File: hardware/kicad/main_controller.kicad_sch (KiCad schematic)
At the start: 40 parts, among them Q4 DMG1012UW, SW2 B3U-3000P, U1 ESP32-C6FH4, Y1 CM315D32768DZFT, Y2 R940000171

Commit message: hardware/kicad/battery.kicad_sch
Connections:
- net ANT_FEED: now reaches AE1.1 (FEED), C24.2, L4.1
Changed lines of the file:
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@@
 (kicad_sch (version 20230121) (generator eeschema)
   (paper "A4")
+  (title_block
+    (date "2023-10-16")
+    (rev "2")
+  )
   (junction (at 19.05 76.2) (diameter 0) (color 0 0 0 0)
   )
@@
     (effects (font (size 1.27 1.27)) (justify right bottom))
   )
+  (label "ANT_FEED" (at 254.635 27.305 0) (fields_autoplaced)
+    (effects (font (size 1.27 1.27)) (justify left bottom))
+  )
   (label "DL_RXD0" (at 149.86 56.515 180) (fields_autoplaced)

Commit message: wip: removing powergate
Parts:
- removed D2 (x2): RB161QS-40T18R, plantpal:D_0402_1005Metric, symbol Diode:MBR0540
- removed R16: 1M, Resistor_SMD:R_0402_1005Metric, symbol Device:R_Small
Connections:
- net RESET_BTN is gone; now on net CHIP_EN: SW2.1, TP3.1
- net DONE: no longer names the net of U1.11 (MTDI/GPIO5/FSPIWP/ADC1_CH5)
- net M_DRVOUT: no longer names the net of U1.10 (MTMS/GPIO4/FSPIHD/ADC1_CH4)
- no-connect marks 0 -> 2
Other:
- note removed: "Protect from other M_DRV source"

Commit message: wip: revision 2
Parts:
- added Q4: DMG1012UW, Package_TO_SOT_SMD:SOT-323_SC-70, symbol Device:Q_NMOS_GSD
- added R13: 10K, Resistor_SMD:R_0402_1005Metric, symbol Device:R_Small
- added R16: 1M, Resistor_SMD:R_0402_1005Metric, symbol Device:R_Small
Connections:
- net +3V3: now also R13.1
- net GND: now also Q4.2 (S), R16.2
- net MPP_STS_READ: now reaches U1.11 (MTDI/GPIO5/FSPIWP/ADC1_CH5)
- net MPP_STS_READ: now also Q4.3 (D), R13.2
- new net MPP_STATUS: Q4.1 (G), R16.1
- no-connect marks 2 -> 1

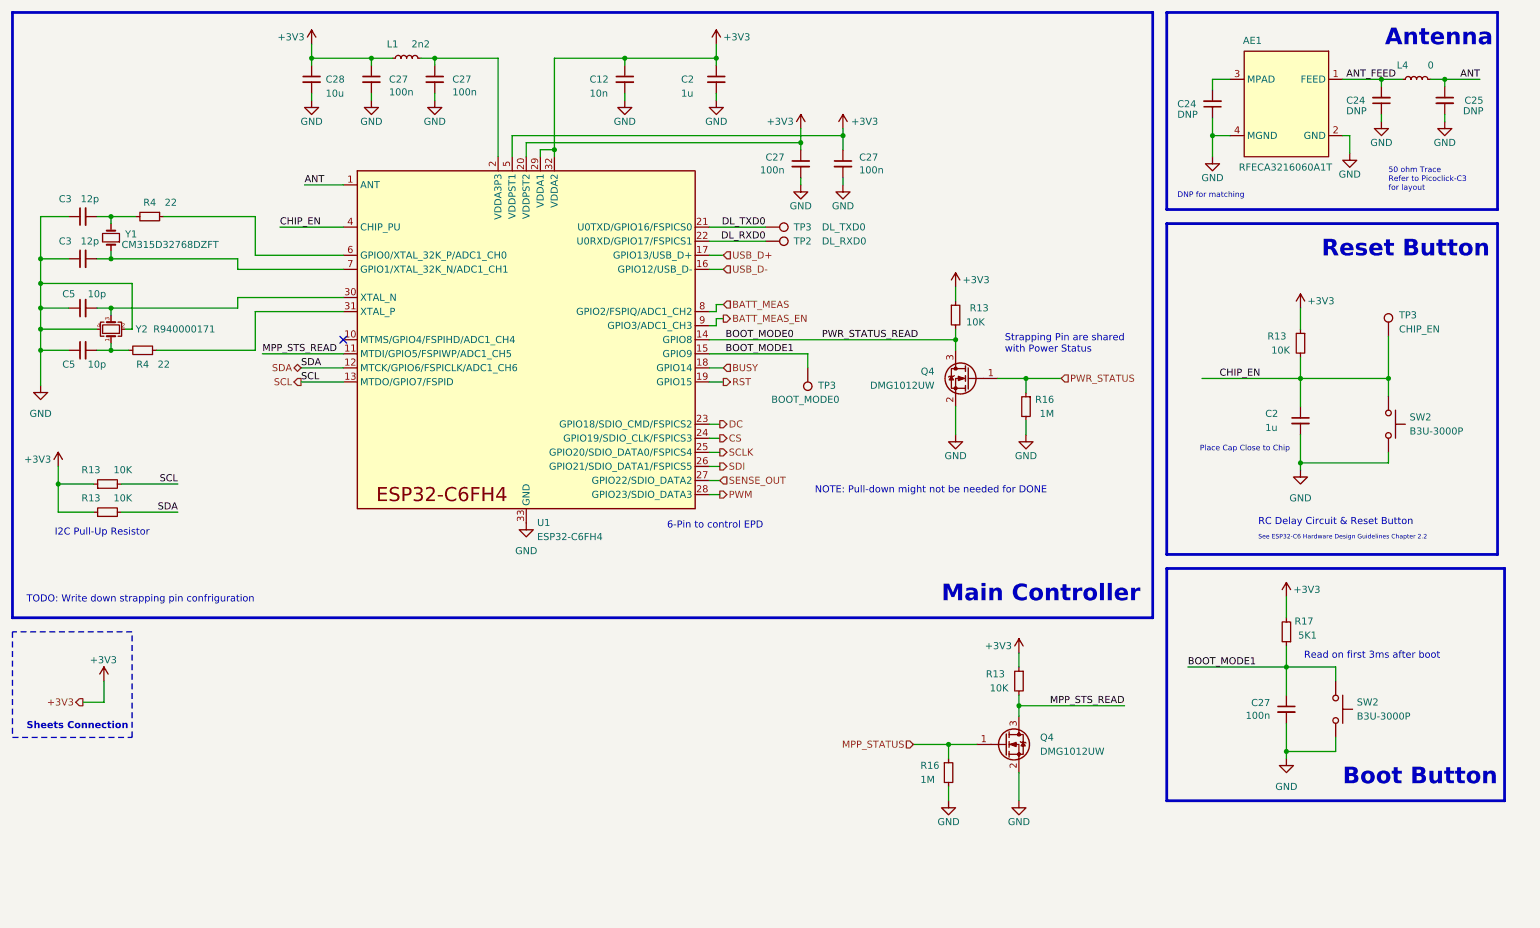
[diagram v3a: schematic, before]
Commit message: re-route sense out, add display power switch
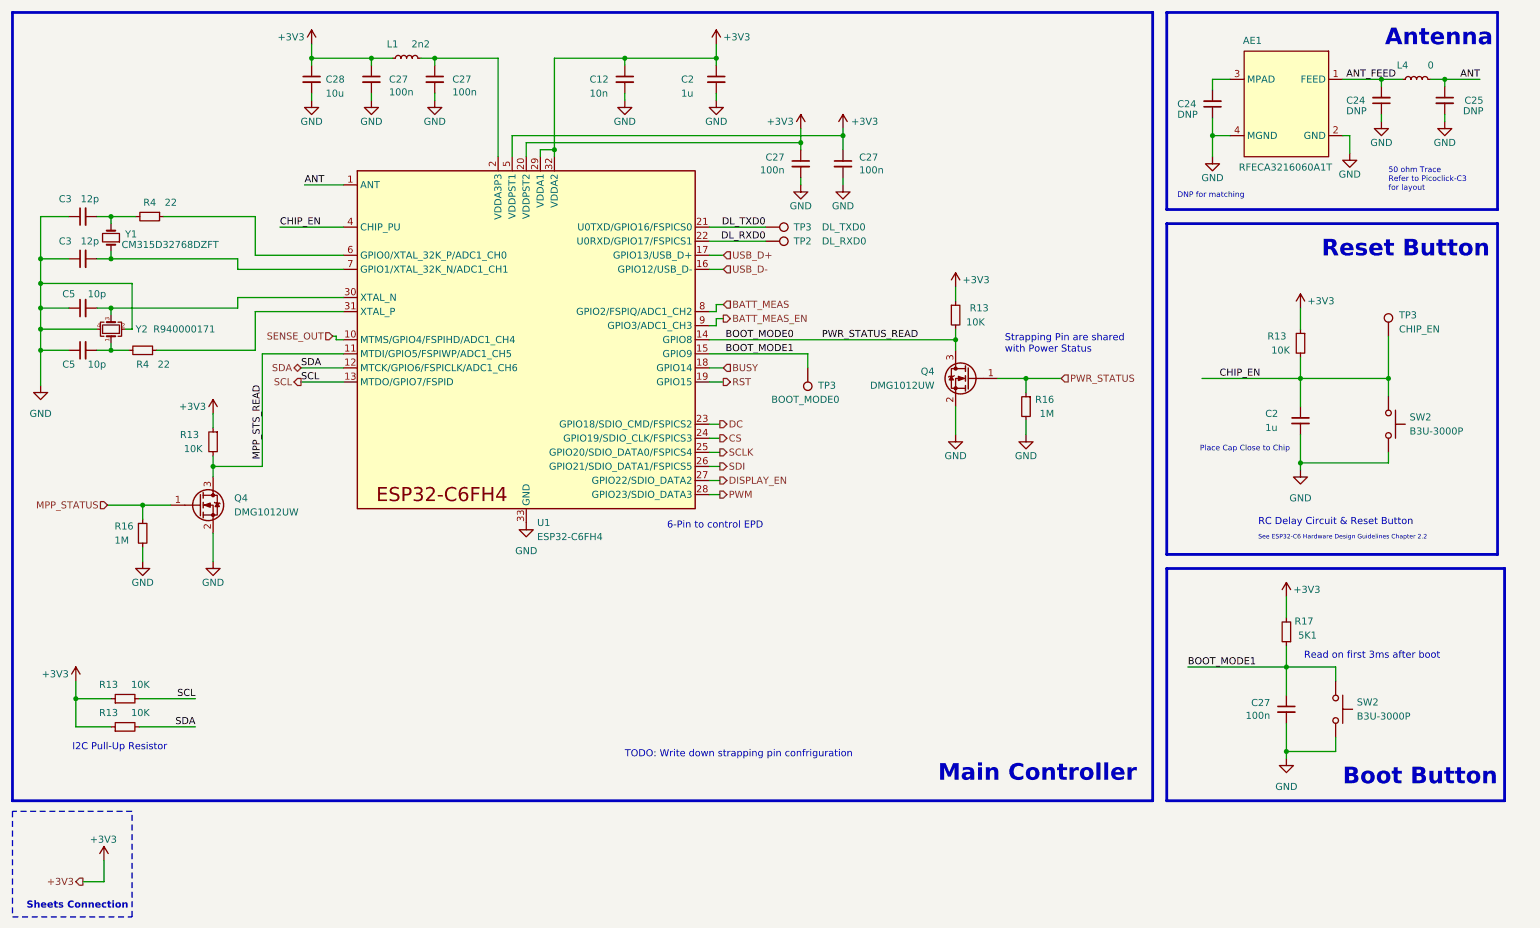
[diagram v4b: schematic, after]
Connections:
- net SENSE_OUT: now also U1.10 (MTMS/GPIO4/FSPIHD/ADC1_CH4); no longer U1.27 (GPIO22/SDIO_DATA2)
- new net DISPLAY_EN: U1.27 (GPIO22/SDIO_DATA2)
- no-connect marks 1 -> 0
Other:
- note removed: "NOTE: Pull-down might not be needed for DONE"
- moved on the sheet: Q4, R13, R16

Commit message: revision 3 prod
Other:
- note removed: "50 ohm Trace Refer to Picoclick-C3 for layout"
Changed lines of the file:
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@@
     (effects (font (size 1 1)) (justify right bottom))
   )
-  (text "TODO: Write down strapping pin confriguration" (at 124.46 149.86 0)
+  (text "TODO: Write down strapping pin confriguration" (at 52.07 154.94 0)
     (effects (font (size 1.27 1.27)) (justify left bottom))
   )
@@
     (effects (font (size 1.27 1.27) (thickness 0.6) bold) (justify left bottom))
   )
-  (text "50 ohm Trace\nRefer to Picoclick-C3 \nfor layout" (at 262.255 47.625 0)
-    (effects (font (size 1 1)) (justify left bottom))
-  )
   (text "Boot Button" (at 254 154.94 0)

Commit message: fix schematic info
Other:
- company: (none) -> Teapot Laboratories
- title: (none) -> Main Controller
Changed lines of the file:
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@@
   (paper "A4")
   (title_block
-    (date "2023-10-16")
-    (rev "2")
+    (title "Main Controller")
+    (date "2024-01-10")
+    (rev "3")
+    (company "Teapot Laboratories")
   )
   (junction (at 19.05 76.2) (diameter 0) (color 0 0 0 0)

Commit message: clean-up
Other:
- note removed: "6-Pin to control EPD"
- note removed: "TODO: Write down strapping pin confriguration"
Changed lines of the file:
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@@
     (effects (font (size 1 1)) (justify right bottom))
-  )
-  (text "TODO: Write down strapping pin confriguration" (at 52.07 154.94 0)
-    (effects (font (size 1.27 1.27)) (justify left bottom))
   )
   (text "Reset Button" (at 250.19 59.69 0)
@@
     (effects (font (size 0.8 0.8)) (justify left bottom))
   )
-  (text "6-Pin to control EPD" (at 132.08 108.585 0)
-    (effects (font (size 1.27 1.27)) (justify left bottom))
-  )
   (text "RC Delay Circuit & Reset Button" (at 238.76 107.95 0)
